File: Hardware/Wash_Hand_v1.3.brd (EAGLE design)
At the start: 71.1 x 48.3 mm, 62 parts, among them IC1 LM358D, IC2 LP298XS, IC3 405016TSSOP, J1 I2C, J2 ICSP, J3 SPI, J4 9V_CONN, J5 EXT_VCC, J6 6_PIN_SERIAL_CABLEPTH, Q1 16.0 Mhz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

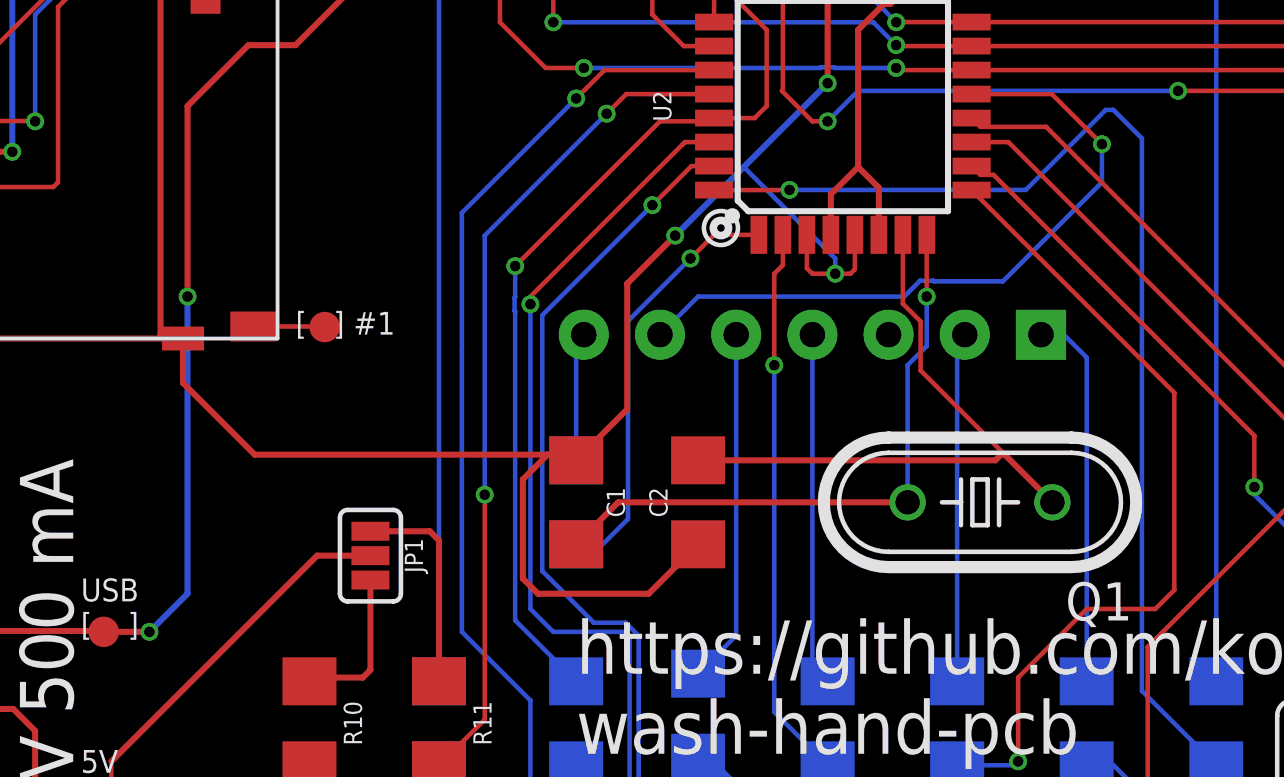
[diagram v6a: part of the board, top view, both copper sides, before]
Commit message: Board/Schematic: Fix the 16MHz/10pF capacitors.
The way they are were in the schematic looked right.
Two capacitors off the crystal. Both capacitors go to
ground. Except that what Eagle decided it should be was:

XTAL1         XTAL2
|             |
+--[CRYSTAL]--+
             [CAP]
              |
             [CAP]
              |
             [GND]

Instead of the:

XTAL1         XTAL2
|             |
+--[CRYSTAL]--+
[CAP]        [CAP]
|             |
\------+------/
     [GND]

This fixes it.

Signed-off-by: Konrad Rzeszutek Wilk <konrad@kernel.org>
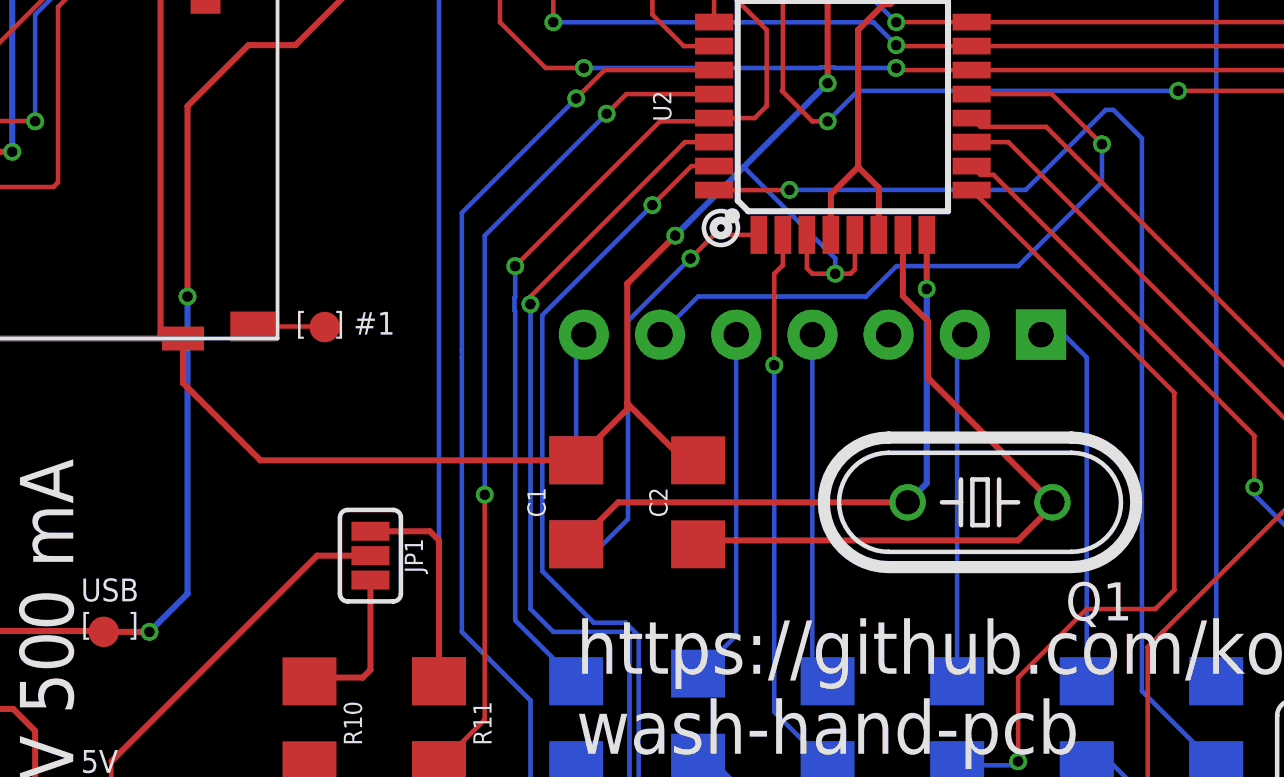
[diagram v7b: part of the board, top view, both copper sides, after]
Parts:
- turned C1 to 90 degrees
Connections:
- net 0: now also C1.2, C2.2; no longer C1.1, C2.1
- net XTAL1: now also C2.1; no longer C2.2
- net XTAL2: now also C1.1; no longer C1.2
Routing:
- net 0: track 343.8 -> 335.8 mm
- net XTAL1: track 21.3 -> 23.4 mm
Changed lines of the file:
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@@
 </autorouter>
 <elements>
-<element name="C1" library="SparkFun-Capacitors" library_urn="urn:adsk.eagle:library:510" package="1206" package3d_urn="urn:adsk.eagle:package:37426/1" value="10pF" x="25.654" y="18.288" smashed="yes" rot="R270">
-<attribute name="NAME" x="26.67" y="18.288" size="0.6096" layer="25" font="vector" ratio="20" rot="R270" align="bottom-center"/>
-<attribute name="PROD_ID" value="CAP-10057" x="-28.956" y="-4.572" size="1.778" layer="27" rot="R270" display="off"/>
-<attribute name="VALUE" value="10uF" x="24.638" y="18.288" size="0.6096" layer="27" font="vector" ratio="20" rot="R270" align="top-center"/>
+<element name="C1" library="SparkFun-Capacitors" library_urn="urn:adsk.eagle:library:510" package="1206" package3d_urn="urn:adsk.eagle:package:37426/1" value="10pF" x="25.654" y="18.288" smashed="yes" rot="R90">
+<attribute name="NAME" x="24.638" y="18.288" size="0.6096" layer="25" font="vector" ratio="20" rot="R90" align="bottom-center"/>
+<attribute name="PROD_ID" value="CAP-10057" x="80.264" y="41.148" size="1.778" layer="27" rot="R90" display="off"/>
+<attribute name="VALUE" value="10uF" x="26.67" y="18.288" size="0.6096" layer="27" font="vector" ratio="20" rot="R90" align="top-center"/>
 </element>
 <element name="C2" library="SparkFun-Capacitors" library_urn="urn:adsk.eagle:library:510" package="1206" package3d_urn="urn:adsk.eagle:package:37426/1" value="10pF" x="29.718" y="18.288" smashed="yes" rot="R90">
@@
 <signal name="0">
 <contactref element="U$4" pad="5"/>
-<contactref element="C2" pad="1"/>
-<contactref element="C1" pad="1"/>
 <contactref element="J" pad="2"/>
 <contactref element="J5" pad="1"/>
@@
 <wire x1="11.938" y1="23.748" x2="4.7" y2="23.748" width="0.2032" layer="1"/>
 <wire x1="4.7" y1="23.748" x2="4.699" y2="23.749" width="0.2032" layer="1"/>
-<wire x1="14.938840625" y1="19.877" x2="12.55" y2="22.265840625" width="0.2032" layer="1"/>
 <wire x1="12.55" y1="23.748" x2="12.55" y2="22.265840625" width="0.2032" layer="1"/>
 <wire x1="4.05" y1="32.098" x2="2.0498" y2="32.098" width="0.1524" layer="1"/>
@@
 <wire x1="56.8198" y1="1.1938" x2="47.8282" y2="1.1938" width="0.2032" layer="1"/>
 <wire x1="47.8282" y1="1.1938" x2="45.974" y2="3.048" width="0.2032" layer="1"/>
-<wire x1="14.938840625" y1="19.877" x2="24.703" y2="19.877" width="0.2032" layer="1"/>
-<wire x1="25.465" y1="19.877" x2="25.654" y2="19.688" width="0.2032" layer="1"/>
-<wire x1="29.718" y1="16.888" x2="28.07" y2="15.24" width="0.2032" layer="1"/>
-<wire x1="28.07" y1="15.24" x2="24.384" y2="15.24" width="0.2032" layer="1"/>
-<wire x1="24.384" y1="15.24" x2="23.876" y2="15.748" width="0.2032" layer="1"/>
-<wire x1="23.876" y1="15.748" x2="23.876" y2="19.05" width="0.2032" layer="1"/>
-<wire x1="23.876" y1="19.05" x2="24.703" y2="19.877" width="0.2032" layer="1"/>
-<wire x1="24.703" y1="19.877" x2="25.465" y2="19.877" width="0.2032" layer="1"/>
 <wire x1="45.466" y1="45.85" x2="46.606" y2="45.85" width="0.2032" layer="1"/>
 <wire x1="46.606" y1="45.85" x2="47.752" y2="44.704" width="0.2032" layer="1"/>
@@
 <wire x1="6.888" y1="11.4" x2="5.42" y2="11.4" width="0.2032" layer="1"/>
 <contactref element="U2" pad="21"/>
-<wire x1="25.654" y1="19.688" x2="27.3558" y2="21.3898" width="0.2032" layer="1"/>
-<wire x1="27.3558" y1="21.3898" x2="27.3558" y2="25.5778" width="0.2032" layer="1"/>
+<wire x1="27.3558" y1="21.59" x2="27.3558" y2="21.3898" width="0.2032" layer="1"/>
+<wire x1="27.3558" y1="21.59" x2="27.3558" y2="25.5778" width="0.2032" layer="1"/>
 <wire x1="27.3558" y1="25.5778" x2="28.956" y2="27.178" width="0.2032" layer="1"/>
 <via x="28.956" y="27.178" extent="1-16" drill="0.35"/>
@@
 <wire x1="34.798" y1="25.908" x2="34.29" y2="25.908" width="0.1524" layer="1"/>
 <wire x1="33.344" y1="27.2034" x2="33.344" y2="26.092" width="0.1524" layer="1"/>
+<contactref element="C2" pad="2"/>
+<contactref element="C1" pad="2"/>
+<wire x1="29.718" y1="19.688" x2="29.2578" y2="19.688" width="0.2032" layer="1"/>
+<wire x1="29.2578" y1="19.688" x2="27.3558" y2="21.59" width="0.2032" layer="1"/>
+<wire x1="27.3558" y1="21.3898" x2="25.654" y2="19.688" width="0.2032" layer="1"/>
+<wire x1="15.127840625" y1="19.688" x2="25.654" y2="19.688" width="0.2032" layer="1"/>
+<wire x1="12.55" y1="22.265840625" x2="15.127840625" y2="19.688" width="0.2032" layer="1"/>
 </signal>
 <signal name="D0">
@@
 <via x="43.18" y="30.226" extent="1-16" drill="0.35"/>
 <wire x1="43.18" y1="30.226" x2="43.18" y2="28.956" width="0.1524" layer="16"/>
-<wire x1="43.18" y1="28.956" x2="39.878" y2="25.654" width="0.1524" layer="16"/>
-<wire x1="37.5577875" y1="25.6766" x2="37.1182125" y2="25.6766" width="0.1524" layer="16"/>
-<wire x1="37.1182125" y1="25.6766" x2="36.5876125" y2="25.146" width="0.1524" layer="16"/>
-<wire x1="39.878" y1="25.654" x2="37.5803875" y2="25.654" width="0.1524" layer="16"/>
-<wire x1="37.5803875" y1="25.654" x2="37.5577875" y2="25.6766" width="0.1524" layer="16"/>
+<wire x1="43.18" y1="28.956" x2="40.386" y2="26.162" width="0.1524" layer="16"/>
+<wire x1="40.386" y1="26.162" x2="36.3336125" y2="26.162" width="0.1524" layer="16"/>
+<wire x1="36.3336125" y1="26.162" x2="35.3176125" y2="25.146" width="0.1524" layer="16"/>
 <wire x1="29.718" y1="25.146" x2="28.448" y2="23.876" width="0.1524" layer="16"/>
-<wire x1="36.5876125" y1="25.146" x2="29.718" y2="25.146" width="0.1524" layer="16"/>
+<wire x1="35.3176125" y1="25.146" x2="29.718" y2="25.146" width="0.1524" layer="16"/>
 </signal>
 <signal name="D3">
@@
 </signal>
 <signal name="XTAL2">
-<contactref element="C1" pad="2"/>
 <contactref element="Q1" pad="2"/>
+<wire x1="27.054" y1="18.288" x2="36.703" y2="18.288" width="0.2032" layer="1"/>
+<wire x1="36.703" y1="18.288" x2="37.338" y2="18.923" width="0.2032" layer="16"/>
+<wire x1="37.338" y1="25.4" x2="37.338" y2="18.923" width="0.2032" layer="16"/>
+<contactref element="U2" pad="8"/>
+<via x="37.338" y="25.4" extent="1-16" drill="0.35"/>
+<wire x1="37.338" y1="25.4" x2="37.338" y2="27.1974" width="0.2032" layer="1"/>
+<wire x1="37.338" y1="27.1974" x2="37.344" y2="27.2034" width="0.1524" layer="1"/>
+<contactref element="C1" pad="1"/>
 <wire x1="25.654" y1="16.888" x2="27.054" y2="18.288" width="0.2032" layer="1"/>
-<wire x1="27.054" y1="18.288" x2="36.703" y2="18.288" width="0.2032" layer="1"/>
-<wire x1="36.703" y1="18.288" x2="36.703" y2="22.86" width="0.1524" layer="16"/>
-<contactref element="U2" pad="8"/>
-<wire x1="36.703" y1="22.86" x2="37.338" y2="23.495" width="0.1524" layer="16"/>
-<wire x1="37.338" y1="23.495" x2="37.338" y2="25.146" width="0.1524" layer="16"/>
-<via x="37.338" y="25.146" extent="1-16" drill="0.35"/>
-<wire x1="37.338" y1="25.146" x2="37.338" y2="27.1974" width="0.1524" layer="1"/>
-<wire x1="37.338" y1="27.1974" x2="37.344" y2="27.2034" width="0.1524" layer="1"/>
 </signal>
 <signal name="XTAL1">
 <contactref element="Q1" pad="1"/>
-<contactref element="C2" pad="2"/>
-<wire x1="41.529" y1="18.288" x2="39.9415" y2="19.8755" width="0.2032" layer="1"/>
-<wire x1="39.9415" y1="19.8755" x2="39.878" y2="19.939" width="0.2032" layer="1"/>
-<wire x1="29.718" y1="19.688" x2="39.627" y2="19.688" width="0.2032" layer="1"/>
-<wire x1="39.627" y1="19.688" x2="39.878" y2="19.939" width="0.2032" layer="1"/>
 <contactref element="U2" pad="7"/>
-<wire x1="37.1348" y1="24.3178875" x2="36.544" y2="24.9086875" width="0.1524" layer="1"/>
-<wire x1="36.544" y1="24.9086875" x2="36.544" y2="27.2034" width="0.1524" layer="1"/>
-<wire x1="39.9415" y1="19.8755" x2="37.1348" y2="22.6822" width="0.1524" layer="1"/>
-<wire x1="37.1348" y1="22.6822" x2="37.1348" y2="24.3178875" width="0.1524" layer="1"/>
+<wire x1="37.3888" y1="24.3178875" x2="36.544" y2="25.1626875" width="0.2032" layer="1"/>
+<wire x1="36.544" y1="25.1626875" x2="36.544" y2="27.2034" width="0.2032" layer="1"/>
+<contactref element="C2" pad="1"/>
+<wire x1="37.3888" y1="22.4282" x2="37.3888" y2="24.3178875" width="0.2032" layer="1"/>
+<wire x1="29.848" y1="17.018" x2="29.718" y2="16.888" width="0.1524" layer="1"/>
+<wire x1="37.3888" y1="22.4282" x2="41.529" y2="18.288" width="0.2032" layer="1"/>
+<wire x1="41.529" y1="18.288" x2="41.529" y2="18.161" width="0.2032" layer="1"/>
+<wire x1="41.529" y1="18.161" x2="40.386" y2="17.018" width="0.2032" layer="1"/>
+<wire x1="40.386" y1="17.018" x2="29.848" y2="17.018" width="0.2032" layer="1"/>
 </signal>
 <signal name="PIN_C">
@@
 <signal name="PIN_B">
 <contactref element="R2" pad="1"/>
-<wire x1="26.416" y1="16.764" x2="27.3812" y2="17.7292" width="0.1524" layer="16"/>
-<wire x1="27.3812" y1="24.3332" x2="27.3812" y2="17.7292" width="0.1524" layer="16"/>
+<wire x1="27.3812" y1="17.7292" x2="26.416" y2="16.764" width="0.1524" layer="16"/>
 <wire x1="25.654" y1="16.888" x2="26.292" y2="16.888" width="0.1524" layer="16"/>
 <wire x1="26.292" y1="16.888" x2="26.416" y2="16.764" width="0.1524" layer="16"/>
 <contactref element="U2" pad="1"/>
-<wire x1="27.3812" y1="24.3332" x2="29.464" y2="26.416" width="0.1524" layer="16"/>
+<wire x1="29.464" y1="26.416" x2="27.3812" y2="24.3332" width="0.1524" layer="16"/>
 <via x="29.464" y="26.416" extent="1-16" drill="0.35"/>
 <wire x1="29.464" y1="26.416" x2="30.2514" y2="27.2034" width="0.1524" layer="1"/>
 <wire x1="30.2514" y1="27.2034" x2="31.744" y2="27.2034" width="0.1524" layer="1"/>
+<wire x1="27.3812" y1="24.3332" x2="27.3812" y2="17.7292" width="0.1524" layer="16"/>
 </signal>
 <signal name="PIN_D">
